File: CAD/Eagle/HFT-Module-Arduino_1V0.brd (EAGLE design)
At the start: 96.5 x 96.5 mm, 29 parts, among them X111 2X20/90_1MM27_HARWIN_M50-3202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, X121 2X20/90_1MM27_HARWIN_M50-3202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

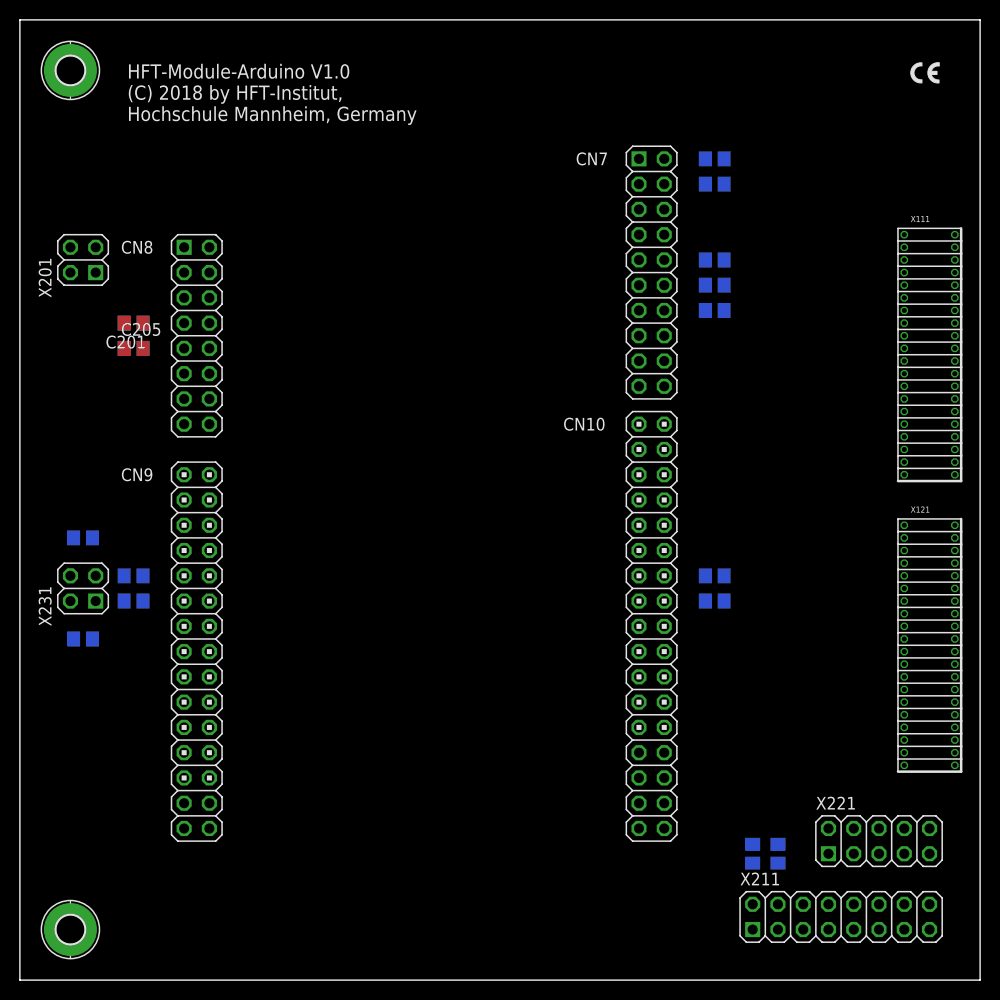
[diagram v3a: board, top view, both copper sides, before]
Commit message: HW_1V0 - CAD/Eagle - placing finished, routing started
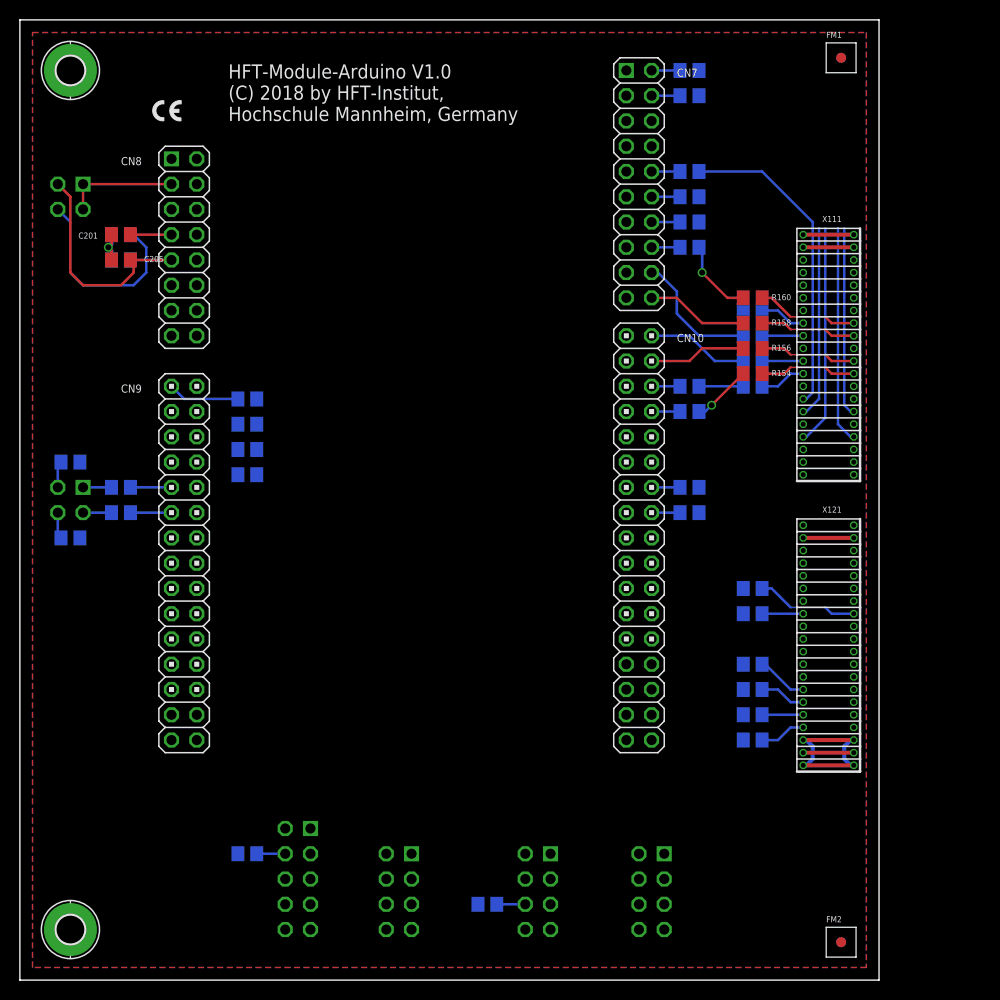
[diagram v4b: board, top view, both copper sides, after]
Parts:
- removed X221: (no value), df4iah_connector:2X05
- added FM1, FM2: (no value), df4iah_fiducial:FIDUCIAL_MARK_1MM
- added R125, R126, R127, R128, R152, R153, R154, R155, R156, R157, R158, R159, R160, R161: 47R, rcl:R0805
- added R324, R334, R335, R341, R342, R343, R344: 0R, rcl:R0805
- added X240, X241, X251: (no value), df4iah_connector:2X04
- X211: device df4iah_connector:2X08 -> df4iah_connector:2X05
- moved X211 54.7 mm to (27.9, 10.2), flipped to the bottom, turned to 270 degrees
- moved R121 50.8 mm to (22.9, 12.7), turned to 0 degrees
- moved R122 29.6 mm to (47.0, 7.62), turned to 0 degrees
- moved R231 17.8 mm to (5.08, 52.1)
- moved X111 10.2 mm to (81.3, 62.2)
- moved X121 10.2 mm to (81.3, 33.0)
- moved R115 9.25 mm to (67.3, 78.7)
- moved R124 9.25 mm to (67.3, 47.0)
- moved R313 9.25 mm to (67.3, 91.4)
- moved R314 9.25 mm to (67.3, 88.9)
- moved R321 9.25 mm to (67.3, 81.3)
- moved R323 9.25 mm to (67.3, 76.2)
- moved R331 9.25 mm to (67.3, 49.5)
- moved C201 8.98 mm to (10.2, 74.9)
- moved C202 8.98 mm to (10.2, 74.9)
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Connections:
- net N$1 renamed SDA_TERM
- net N$2 renamed SCL_TERM
- new net D10: R160.1, R324.2
- new net D11: R161.1, X211.2, X240.2, X241.2
- new net D2: R152.1, X211.10, X240.8
- new net D3: R153.1, X211.8, X241.8
- new net D4: R154.1, R334.2
- new net D5: R155.1, R335.2
- new net EXP_PX0_INOUT_R: R128.2, X121.33
- new net EXP_PX1_INOUT_R: R127.2, X121.31
- new net EXP_PX2_INOUT_R: R126.2, X121.29
- new net EXP_PX3_INOUT_R: R125.2, X121.27
- net A0: now also R341.2
- net A1: now also R342.2
- net A2: now also R343.2
- net A3: now also R344.2
- net D10_SS: now also R324.1; no longer X221.1, X221.3, X221.5, X221.7, X221.9
- net D2_INT0: now also X240.1, X240.3, X240.5, X240.7, X251.7
- net D3_INT1: now also X241.1, X241.3, X241.5, X241.7, X251.5
- net D4_T0: now also R334.1, X251.3
- net D5_T1: now also R335.1, X251.1
- net D6: now also R156.1
- net D7: now also R157.1
- net D8: now also R158.1
- net D9: now also R159.1
- net EXP_I2S_MSR_FS_OUT_R: now also R160.2
- net EXP_I2S_MSR_MCLK_OUT_R: now also R161.2
- net EXP_I2S_MSR_SCK_OUT_R: now also R159.2
- net EXP_I2S_MSR_SD_OUT_R: now also R158.2
- net EXP_I2S_SLV_FS_IN: now also R156.2
- net EXP_I2S_SLV_MCLK_IN: now also R157.2
- net EXP_I2S_SLV_SCK_IN: now also R155.2
- net EXP_I2S_SLV_SD_IN: now also R154.2
- net EXP_PX0_INOUT: now also R128.1, R341.1; no longer X121.33, X211.14, X221.8
- net EXP_PX1_INOUT: now also R127.1, R342.1; no longer X121.31, X211.12, X221.6
- net EXP_PX2_INOUT: now also R126.1, R343.1; no longer X121.29, X211.10, X221.4
- net EXP_PX3_INOUT: now also R125.1, R344.1; no longer X121.27, X211.8, X221.2
- net EXP_TMRCAPT_OUT: now also X240.6, X241.6, X251.2, X251.4, X251.6, X251.8; no longer X211.4
- net EXP_UART_CTS_IN: now also R153.2
- net EXP_UART_RTS_OUT_R: now also R152.2
- net EXP_WAKEUP_OUT: now also X211.4, X240.4, X241.4; no longer X211.2
- net NRST: no longer X211.11, X211.13, X211.15
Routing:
- net +3V3: track 0.00 -> 38.6 mm
- net EXP_SPI_SCK_IN: track 0.00 -> 31.9 mm
- net +5V0: track 0.00 -> 31.7 mm
- net GND: track 0.00 -> 28.3 mm, vias 0 -> 1
- net EXP_I2C_SCL_IN: track 0.00 -> 24.9 mm
- net EXP_I2C_SDA_INOUT: track 0.00 -> 24.7 mm
- net EXP_SPI_MOSI_IN: track 0.00 -> 19.3 mm
- net EXP_SPI_MISO_OUT_R: track 0.00 -> 19.0 mm
- net D9: track 0.00 -> 13.1 mm
- net IOREF: track 0.00 -> 11.4 mm
- net EXP_UART_RTS_OUT_R: track 0.00 -> 10.3 mm
- net D7: track 0.00 -> 10.3 mm
- net EXP_I2S_MSR_FS_OUT_R: track 0.00 -> 10.3 mm
- net D8: track 0.00 -> 10.3 mm
- net EXP_I2S_MSR_SD_OUT_R: track 0.00 -> 9.74 mm
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- added copper zone on layer 1, net GND
- added copper zone on layer 16, net GND
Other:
- board size 96.5 x 96.5 mm -> 86.4 x 96.5 mm
- board text removed: "Position Archer-Headers in mil: TOP x: 3800 - 200, y: 2450 BOT x: 3800 - 200, y: 1300"
